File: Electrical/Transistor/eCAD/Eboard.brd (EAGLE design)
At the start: 71.1 x 56.8 mm, 22 parts

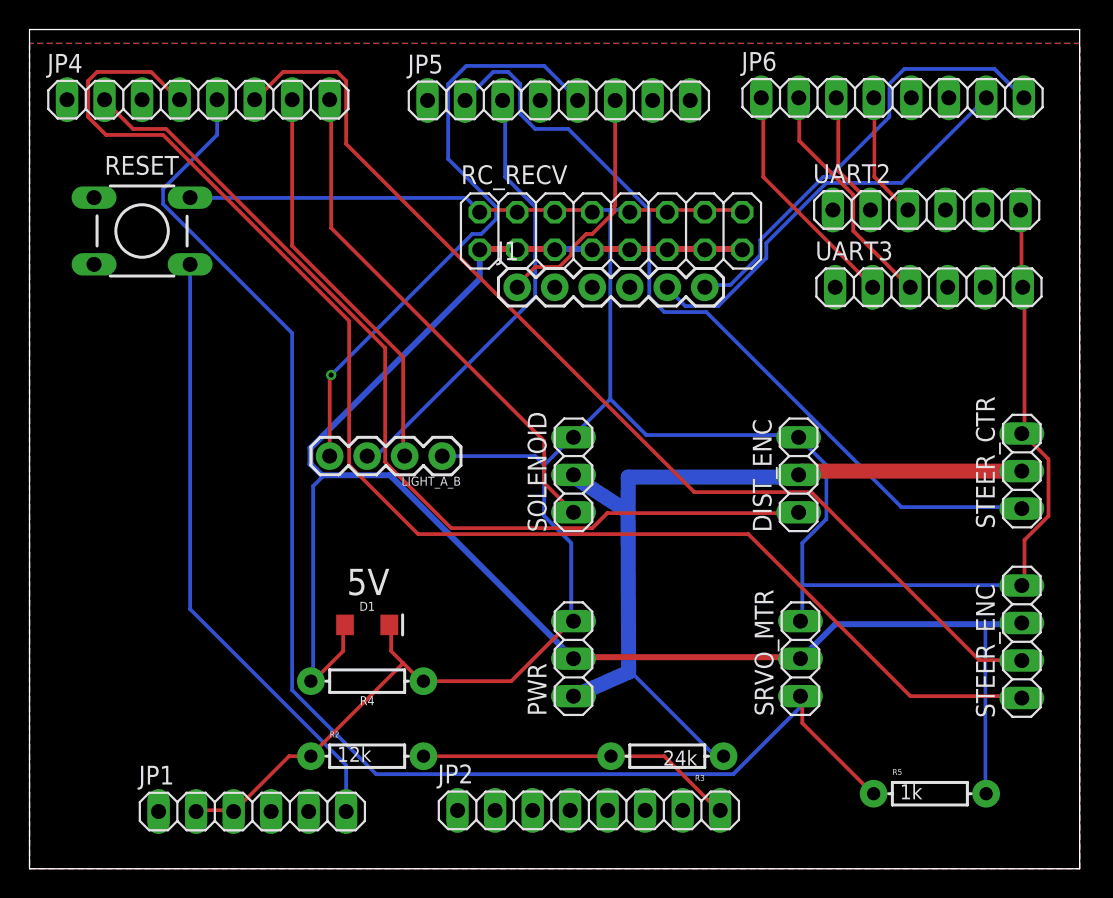
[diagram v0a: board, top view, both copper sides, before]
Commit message: put resistor in series and resolved trace issues on board
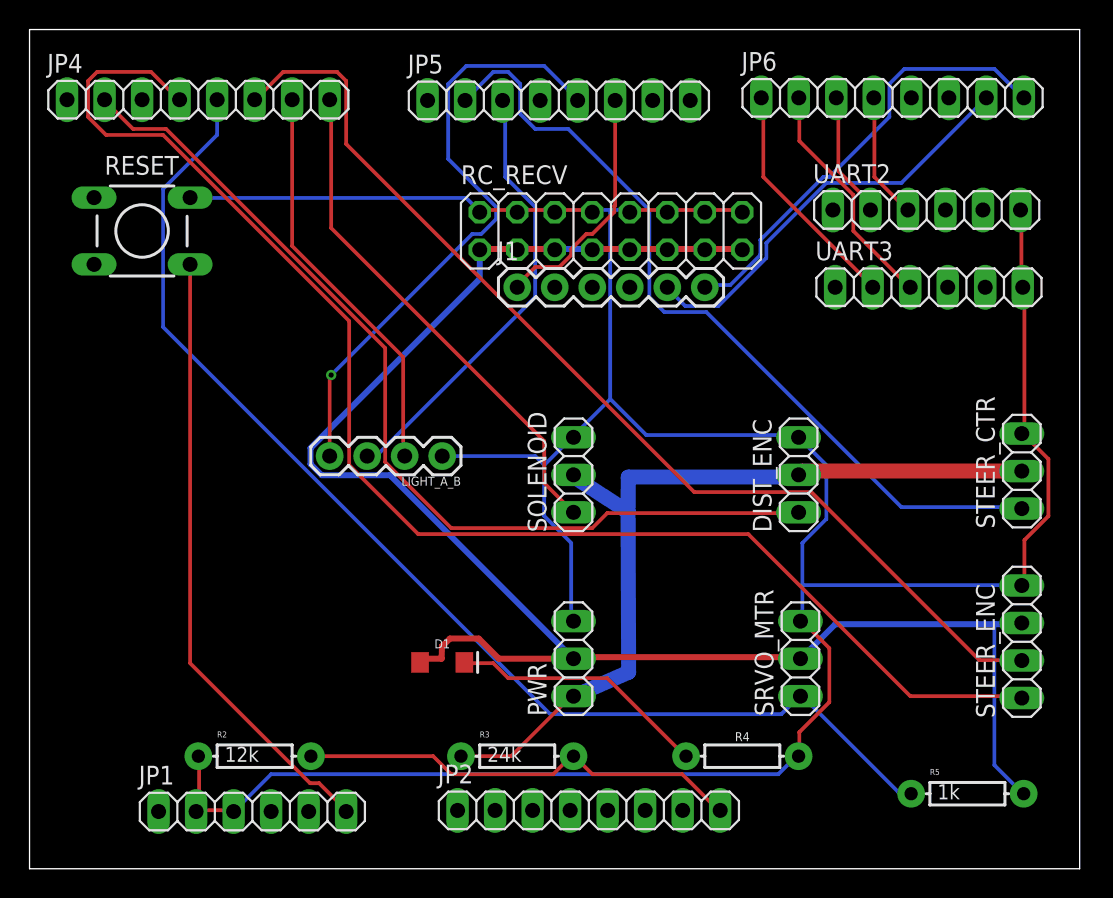
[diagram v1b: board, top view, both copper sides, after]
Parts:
- moved R4 25.9 mm to (50.8, 50.8), turned to 0 degrees
- moved R3 10.2 mm to (35.6, 50.8), turned to 0 degrees
- moved R2 7.62 mm to (17.8, 50.8)
- moved D1 5.68 mm to (30.5, 57.1)
- moved R5 2.54 mm to (66.0, 48.3)
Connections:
- new net N$1: D1.C, R4.P$1
- net 5V: no longer R4.P$2
- net GND: now also R4.P$2; no longer D1.C, R4.P$1
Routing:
- net GND: track 182.0 -> 204.3 mm
- net N$1: track 0.00 -> 17.6 mm
- net SRVO_MTR: track 93.3 -> 81.7 mm
- net VBATT_ADC: track 21.6 -> 30.2 mm
- net 5V: track 123.0 -> 116.7 mm
- net 12V: track 57.4 -> 57.9 mm
- removed copper zone on layer 16, net N$1
- removed copper zone on layer 1, net N$2
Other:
- board text removed: "5V"

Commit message: changed indicator to have pull up resistor in series that has resistance of 60, changed traces to be right size, added 5V silkscreen for indicator led
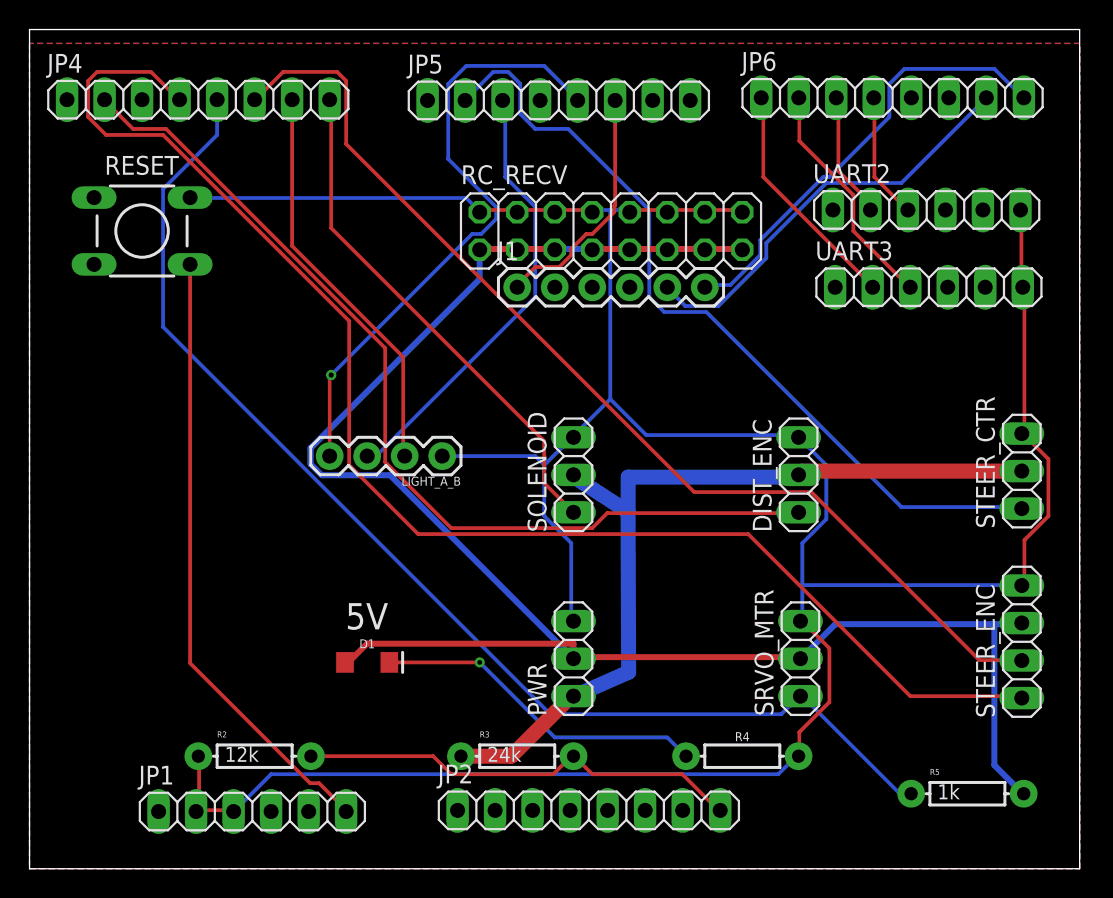
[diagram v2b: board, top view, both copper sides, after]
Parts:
- R4: value 1k -> 60
- moved D1 5.08 mm to (25.4, 57.1)
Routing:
- net N$1: track 17.6 -> 22.7 mm, vias 0 -> 1
- net 5V: track 116.7 -> 121.6 mm
- added copper zone on layer 1, net N$2
- added copper zone on layer 16, net N$3
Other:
- board text added: "5V"
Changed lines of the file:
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@@
 <text x="55.88" y="76.2" size="1.778" layer="26" rot="MR0">ROBOBUGGY
 REV 1.7</text>
+<text x="23.9268" y="59.3852" size="1.778" layer="25">5V</text>
 </plain>
 <attributes>
@@
 </autorouter>
 <elements>
-<element name="D1" library="SparkFun-LED" library_urn="urn:adsk.eagle:library:529" package="LED-1206" package3d_urn="urn:adsk.eagle:package:39352/1" value="" x="30.48" y="57.15"/>
+<element name="D1" library="SparkFun-LED" library_urn="urn:adsk.eagle:library:529" package="LED-1206" package3d_urn="urn:adsk.eagle:package:39352/1" value="" x="25.4" y="57.15"/>
 <element name="DIST_ENC" library="pinhead" package="1X03" value="" x="54.61" y="69.85" rot="R90"/>
 <element name="J1" library="SparkFun-Connectors" package="1X06" value="" x="35.56" y="82.55">
@@
 <attribute name="PROD_ID" value="RES-08380" x="35.56" y="50.8" size="1.778" layer="27" display="off"/>
 </element>
-<element name="R4" library="SparkFun-Resistors" library_urn="urn:adsk.eagle:library:532" package="AXIAL-0.3" package3d_urn="urn:adsk.eagle:package:39658/1" value="1k" x="50.8" y="50.8">
+<element name="R4" library="SparkFun-Resistors" library_urn="urn:adsk.eagle:library:532" package="AXIAL-0.3" package3d_urn="urn:adsk.eagle:package:39658/1" value="60" x="50.8" y="50.8">
 <attribute name="PROD_ID" value="RES-08380" x="50.8" y="50.8" size="1.778" layer="27" display="off"/>
 </element>
@@
 <wire x1="22.323425" y1="69.8246" x2="26.9494" y2="69.8246" width="0.4064" layer="16"/>
 <wire x1="26.9494" y1="69.8246" x2="39.37" y2="57.404" width="0.4064" layer="16"/>
-<wire x1="30.4656" y1="58.2287625" x2="30.472221875" y2="58.235384375" width="0.4064" layer="1"/>
-<wire x1="30.472221875" y1="58.235384375" x2="30.47249375" y2="58.244771875" width="0.4064" layer="1"/>
-<wire x1="30.47249375" y1="58.244771875" x2="30.635175" y2="58.3983375" width="0.4064" layer="1"/>
-<wire x1="34.3191625" y1="57.404" x2="39.37" y2="57.404" width="0.4064" layer="1"/>
-<wire x1="30.635175" y1="58.3983375" x2="31.0012375" y2="58.7644" width="0.4064" layer="1"/>
-<wire x1="31.0012375" y1="58.7644" x2="32.9587625" y2="58.7644" width="0.4064" layer="1"/>
-<wire x1="32.9587625" y1="58.7644" x2="34.3191625" y2="57.404" width="0.4064" layer="1"/>
-<wire x1="29.234" y1="57.404" x2="30.44183125" y2="57.404" width="0.4064" layer="1"/>
-<wire x1="30.44183125" y1="57.404" x2="30.4656" y2="58.2287625" width="0.4064" layer="1"/>
 <contactref element="D1" pad="A"/>
-<wire x1="29.0576" y1="57.3024" x2="28.98" y2="57.15" width="0.254" layer="1"/>
-<wire x1="29.0576" y1="57.3024" x2="29.234" y2="57.404" width="0.254" layer="1"/>
-<wire x1="67.8688" y1="50.1904" x2="67.8688" y2="59.7408" width="0.254" layer="16"/>
-<wire x1="69.6976" y1="48.3616" x2="67.8688" y2="50.1904" width="0.254" layer="16"/>
+<wire x1="67.8688" y1="50.1904" x2="67.8688" y2="59.7408" width="0.4064" layer="16"/>
+<wire x1="69.6976" y1="48.3616" x2="67.8688" y2="50.1904" width="0.4064" layer="16"/>
 <wire x1="69.6976" y1="48.3616" x2="69.85" y2="48.26" width="0.254" layer="16"/>
+<wire x1="25.4" y1="58.42" x2="24.13" y2="57.15" width="0.4064" layer="1"/>
+<wire x1="39.37" y1="58.42" x2="25.4" y2="58.42" width="0.4064" layer="1"/>
+<wire x1="39.37" y1="57.404" x2="39.37" y2="58.42" width="0.4064" layer="1"/>
+<wire x1="24.13" y1="57.15" x2="23.9" y2="57.15" width="0.254" layer="1"/>
 </signal>
 <signal name="GND">
@@
 <wire x1="54.864" y1="70.104" x2="69.723" y2="70.104" width="1.016" layer="1"/>
 <wire x1="54.61" y1="69.85" x2="54.864" y2="70.104" width="1.016" layer="1"/>
-<wire x1="35.1536" y1="50.8" x2="31.75" y2="50.8" width="0.254" layer="1"/>
-<wire x1="39.2176" y1="54.864" x2="35.1536" y2="50.8" width="0.254" layer="1"/>
+<wire x1="35.1536" y1="50.8" x2="31.75" y2="50.8" width="1.016" layer="1"/>
+<wire x1="39.2176" y1="54.864" x2="35.1536" y2="50.8" width="1.016" layer="1"/>
 <wire x1="39.2176" y1="54.864" x2="39.37" y2="54.864" width="0.254" layer="1"/>
 </signal>
@@
 <contactref element="R4" pad="P$1"/>
 <contactref element="D1" pad="C"/>
-<wire x1="33.9344" y1="57.0992" x2="32.1056" y2="57.0992" width="0.254" layer="1"/>
-<wire x1="34.9504" y1="56.0832" x2="33.9344" y2="57.0992" width="0.254" layer="1"/>
-<wire x1="41.656" y1="56.0832" x2="34.9504" y2="56.0832" width="0.254" layer="1"/>
-<wire x1="46.9392" y1="50.8" x2="41.656" y2="56.0832" width="0.254" layer="1"/>
-<wire x1="32.1056" y1="57.0992" x2="31.98" y2="57.15" width="0.254" layer="1"/>
-<wire x1="46.9392" y1="50.8" x2="46.99" y2="50.8" width="0.254" layer="1"/>
+<wire x1="33.02" y1="57.15" x2="26.9" y2="57.15" width="0.254" layer="1"/>
+<wire x1="38.1" y1="52.07" x2="33.02" y2="57.15" width="0.254" layer="16"/>
+<wire x1="45.72" y1="52.07" x2="38.1" y2="52.07" width="0.254" layer="16"/>
+<wire x1="46.99" y1="50.8" x2="45.72" y2="52.07" width="0.254" layer="16"/>
+<via x="33.02" y="57.15" extent="1-16" drill="0.3302"/>
+</signal>
+<signal name="N$2">
+<polygon width="0.1524" layer="1">
+<vertex x="2.54" y="99.06"/>
+<vertex x="2.54" y="43.18"/>
+<vertex x="73.66" y="43.18"/>
+<vertex x="73.66" y="99.06"/>
+</polygon>
+</signal>
+<signal name="N$3">
+<polygon width="0.1524" layer="16">
+<vertex x="2.54" y="99.06"/>
+<vertex x="2.54" y="43.18"/>
+<vertex x="73.66" y="43.18"/>
+<vertex x="73.66" y="99.06"/>
+</polygon>
 </signal>
 </signals>

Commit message: verified edge dimensions on the board and that the board followed oshpark drc rules before doing top and bottom ground fills for board
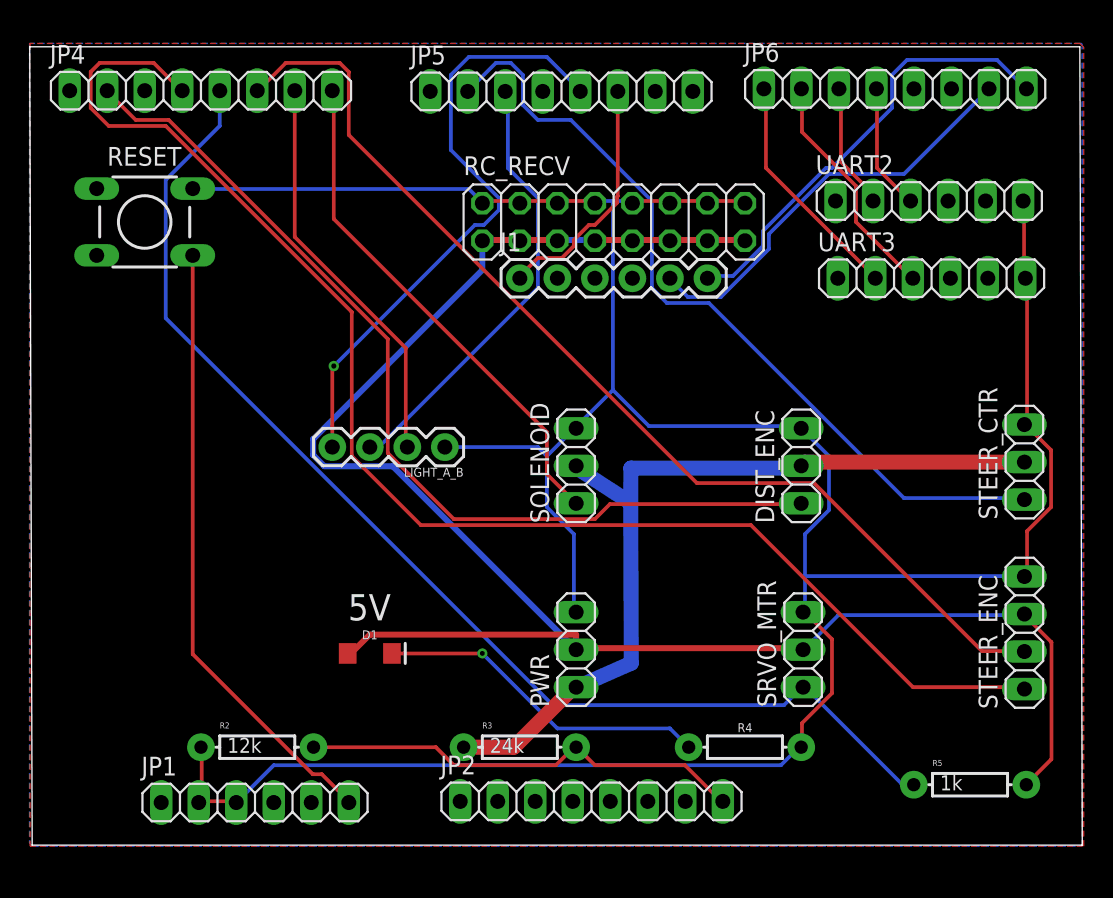
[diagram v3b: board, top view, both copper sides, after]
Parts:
- moved JP5 0.64 mm to (38.6, 95.8)
- moved R4 0.64 mm to (51.0, 51.4)
- moved RC_RECV 0.64 mm to (42.1, 87.0)
- moved SOLENOID 0.64 mm to (39.5, 70.5)
- moved STEER_CTR 0.64 mm to (69.9, 70.7)
- moved STEER_ENC 0.64 mm to (69.9, 59.2)
- moved D1 0.64 mm to (25.6, 57.8)
- moved LIGHT_A_B 0.64 mm to (30.7, 71.7)
- moved JP4 0.64 mm to (14.1, 95.9)
- moved RESET 0.64 mm to (10.3, 87.0)
- moved DIST_ENC 0.63 mm to (54.8, 70.5)
- moved J1 0.63 mm to (35.7, 83.2)
- moved JP1 0.63 mm to (17.8, 47.7)
- moved JP2 0.63 mm to (40.6, 47.7)
- moved JP6 0.63 mm to (61.2, 96.0)
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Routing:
- net 5V: track 121.6 -> 122.3 mm
- added copper zone on layer 16, net N$2
- added copper zone on layer 1, net N$3
- removed copper zone on layer 1, net N$2
- removed copper zone on layer 16, net N$3
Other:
- board size 71.1 x 56.8 mm -> 71.3 x 54.1 mm

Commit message: updated dimensions, reversed the JP1 pin set, reversed JP2 so that VBATT would be in pin A0, reversed all thre three-pin connections to match existing pin plug in configuration, updated R4 resistor to be 120 ohms, switched encA and encB positions
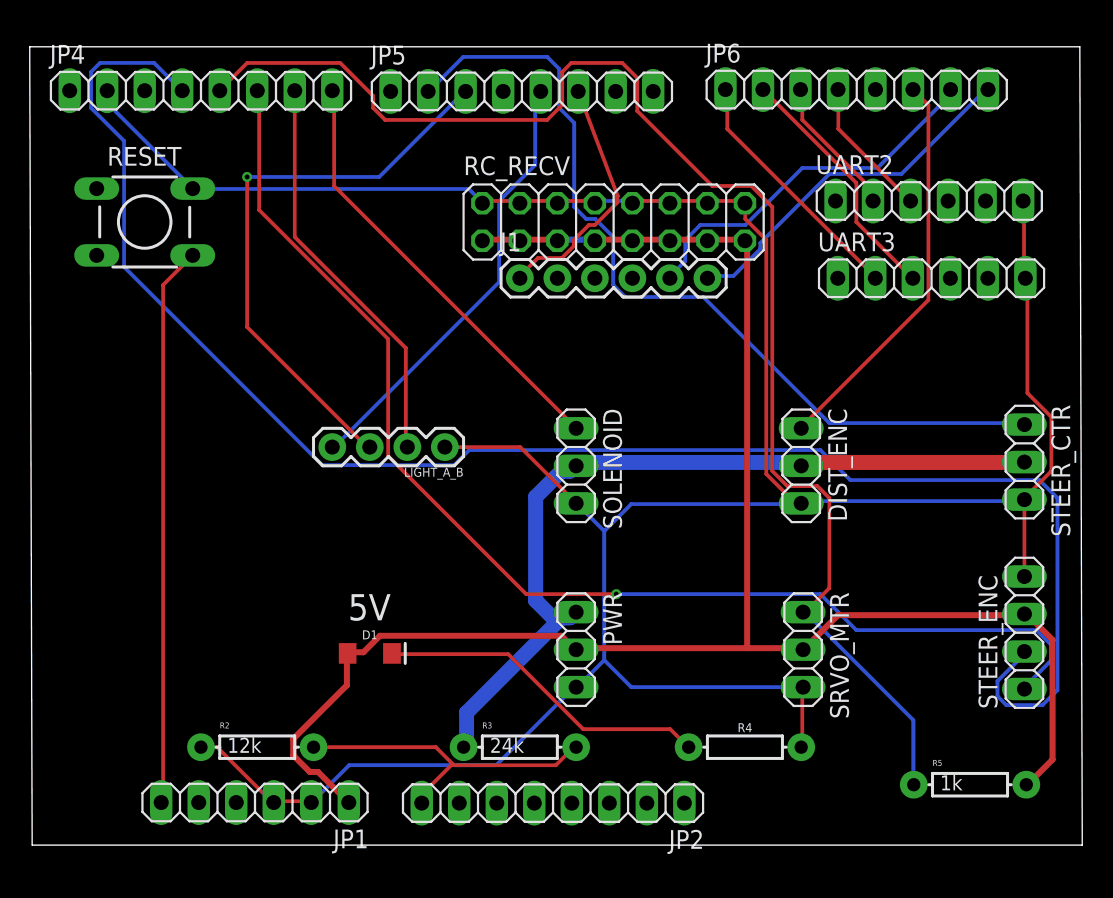
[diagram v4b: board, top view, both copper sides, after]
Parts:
- R4: value 60 -> 120
- moved JP5 2.68 mm to (35.9, 95.8)
- moved JP2 2.61 mm to (38.0, 47.6), turned to 180 degrees
- moved JP6 2.60 mm to (58.5, 95.9)
- turned DIST_ENC to 270 degrees
- turned JP1 to 180 degrees
- turned PWR to 270 degrees
- turned SOLENOID to 270 degrees
- turned SRVO_MTR to 270 degrees
- turned STEER_CTR to 270 degrees
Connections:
- net 5V: now also JP1.1
- net DIST_ENC: now also JP6.6; no longer JP4.2
- net GND: now also JP4.2
- net STEER_ENC1: now also JP4.6; no longer JP4.4
- net STEER_ENC2: now also JP4.4; no longer JP4.6
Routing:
- net STEER_ENC2: track 71.7 -> 113.4 mm
- net DIST_ENC: track 64.0 -> 26.9 mm
- net SRVO_MTR: track 81.7 -> 94.5 mm
- net STEER_ENC1: track 94.9 -> 82.3 mm, vias 0 -> 1
- net LIGHT_1: track 41.8 -> 30.1 mm, vias 1 -> 0
- net LIGHT_2: track 30.1 -> 39.0 mm, vias 0 -> 1
- net VBATT_ADC: track 30.2 -> 22.3 mm
- net BRAKE_RC: track 30.5 -> 24.5 mm
- net SOLENOID: track 34.8 -> 29.7 mm
- net GND: track 204.3 -> 200.0 mm
- net SWITCH: track 41.8 -> 37.9 mm
- net AUTON_RC: track 28.6 -> 25.4 mm
- net STEER_CTR: track 55.4 -> 58.5 mm
- net 12V: track 57.9 -> 56.1 mm
- net 5V: track 122.3 -> 120.9 mm
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- removed copper zone on layer 16, net N$2
- removed copper zone on layer 1, net N$3
